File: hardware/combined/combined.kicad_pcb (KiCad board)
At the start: 2 copper layers, 62 x 208.5 mm, 149 parts, among them J1 USB-C 5V in, J2 Mini-DIN-8 to printer, J4 Mini-DIN-8 LocalTalk, SW1 TSB001A3518A, SW2 B3U-1000P, SW3 TS-1002-BR15026, U1 ESP32-S3-WROOM-1-N8R2, U2 SP3490EN-L, U3 SP3232EBEN-L/TR, U4 AP7361C-33E, U5 USBLC6-2SC6, U6 SP3485EN-L, U7 PIC12F1840-I/P, U8 SP3485EN-L, U9 SN74LV1T125DCKR

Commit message: Rev 2026.11: U1 is the ESP32-S3-WROOM-1-N16R8 (W-1091)
Wells picked the N16R8: 16 MB of flash and 8 MB of octal PSRAM against rev
A's 8 MB and 2 MB, so the firmware has room to grow and a job can buffer a
whole photo page. Its PSRAM takes IO35-IO37, which dropping the DIPs freed;
the netlist gate keeps them off every net. It needs its own firmware build
(W-1109) and is rated to 65 C.

r13_sync.py now also copies the Description, Manufacturer and Datasheet
fields, so the board has no field-parity warnings (R9's stale DNP note
went with them).

Refs: W-1091
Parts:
- U1: value ESP32-S3-WROOM-1-N8R2 -> ESP32-S3-WROOM-1-N16R8

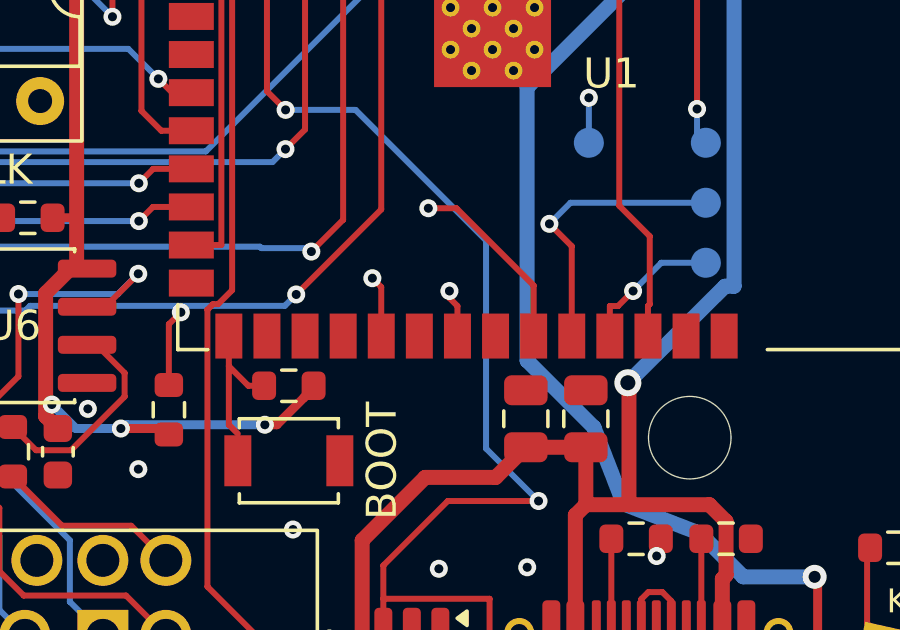
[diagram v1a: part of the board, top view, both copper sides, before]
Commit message: Rev 2026.11: spare pins IO38-IO40 on bare pads; cleanup sees through via stubs (W-1091)
IO38, IO39 and IO40 each run straight down to a via and a bare 1 mm pad on
the back (TP10-TP12, labelled), so a future idea can be tried on a built
board with a few wires. On the back, the front keeps only a short stub per
pin and its ground pour still reaches C1 and C22. IO41 has no way past
USB D- and IO42 has C1 over it.

r13_clean.py no longer counts a stub lying wholly inside a via as joining
it: rev A's DIP and IO35 runs ended so, and the pair held each other up,
leaving dead stubs on IO38, IO40 and IO42. r13_reroute.py's explicit IO35
drops go with it. All other copper is unchanged.

Refs: W-1091
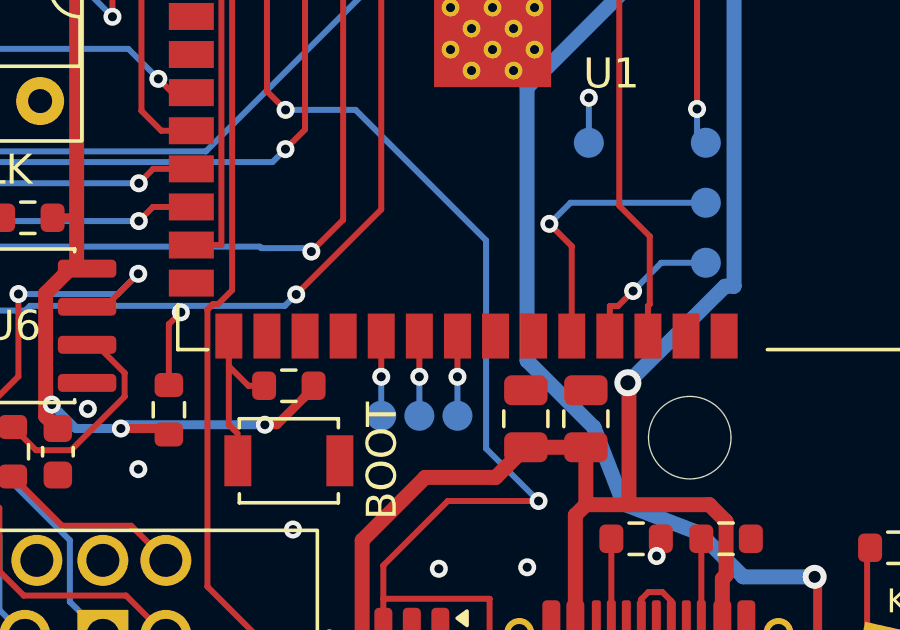
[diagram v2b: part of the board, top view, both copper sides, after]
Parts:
- added TP10: SPARE_IO38, SparePad_D1.0mm, B.Cu at (143.1, 151.2)
- added TP11: SPARE_IO39, SparePad_D1.0mm, B.Cu at (144.3, 151.2)
- added TP12: SPARE_IO40, SparePad_D1.0mm, B.Cu at (145.6, 151.2)
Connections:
- U1 pad 31: unconnected-(U1-IO38-Pad31) -> /SPARE_IO38
- U1 pad 32: unconnected-(U1-IO39-Pad32) -> /SPARE_IO39
- U1 pad 33: unconnected-(U1-IO40-Pad33) -> /SPARE_IO40
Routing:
- net unconnected-(U1-IO42-Pad35): track 6.44 -> 0.00 mm, vias 1 -> 0
- net /SPARE_IO40: track 0.00 -> 2.66 mm, vias 0 -> 1
- net /SPARE_IO39: track 0.00 -> 2.66 mm, vias 0 -> 1
- net /SPARE_IO38: track 0.00 -> 2.66 mm, vias 0 -> 1
- net unconnected-(U1-IO38-Pad31): track 2.25 -> 0.00 mm, vias 1 -> 0
- net unconnected-(U1-IO40-Pad33): track 1.79 -> 0.00 mm, vias 1 -> 0

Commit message: Rev 2026.11: U2 is the THVD1451 (W-1091)
TI's THVD1451DR replaces the SP3490 on the printer port: the same SOIC-8
pinout (checked against TI's SLLSEY3E), +-30 kV HBM on the bus pins
against +-2 kV, and a receiver that works with +-15 V on its inputs, so
an RS-232 printer's line is in range without a divider. R29/R30 stay at
15 k as series protection; a -15 V line lands near -12.5 V. Its
fail-safe threshold reads an idle or unplugged line as mark. Board copper
is unchanged.

Refs: W-1091
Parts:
- U2: value SP3490EN-L -> THVD1451DR

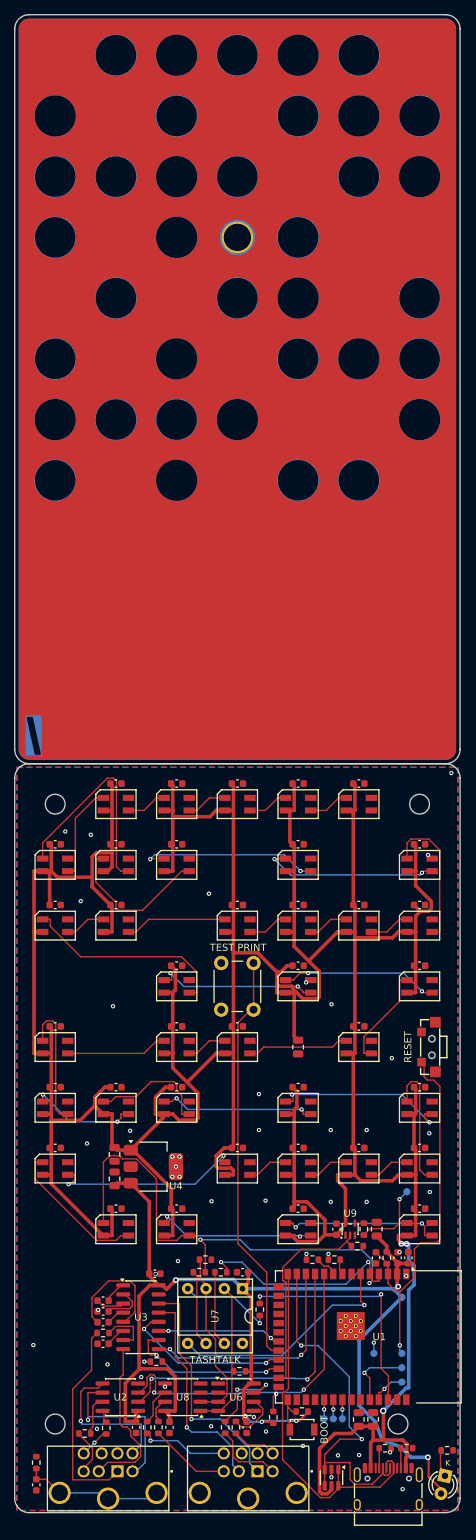
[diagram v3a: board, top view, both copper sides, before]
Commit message: Panel: Frame 16 art, rev 2026.11 (W-1091)
Wells's Frame 16 export, with only its dot area left out: the dots are the
committed ones, pixel for pixel. The rest is Frame 16's: "rev 2026.11", the
text block a few pixels left and up, the port labels on one baseline, and a
power slash of about 1.0 x 5.75 mm (was 0.8 x 5.2), centred 0.3 mm further up.
D3 stays where it is: it can't go west of J1's courtyard, and its 3 mm face
still covers the slash's width. The lattice's D3 tube is re-cut round the new
window (131 tests pass); the combined panel and fab package are rebuilt.

Refs: W-1091
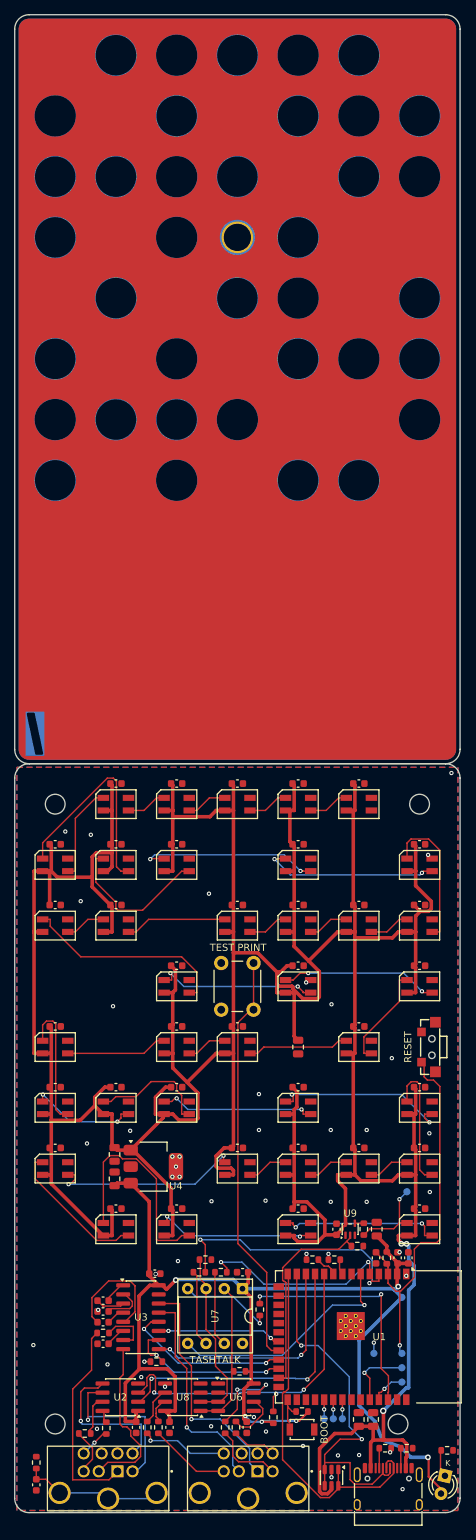
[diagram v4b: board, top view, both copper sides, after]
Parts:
- moved MT2 86.3 mm to (105.6, -38.6)
- moved MT3 86.3 mm to (156.4, 47.7)
- moved MT1 50.7 mm to (156.4, -38.6)
- moved MT4 47.7 mm to (108.6, 47.7)
- renumbered MT2 to MT1, MT4 to MT2, MT1 to MT3, MT3 to MT4

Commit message: Board: WW mark and OSHW logo on the top silk (W-1091)
Where the DIP switch was, at the west edge, where the Lite's clear lid
shows them: the Macintosh Mini board's WW chevrons, 7 mm wide, above
KiCad's 7.5 x 8 mm OSHW logo (a board-only footprint). Copper unchanged;
r13_check.py now checks both are there.

Refs: W-1091
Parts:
- added LOGO1: OSHW-Logo_7.5x8mm_SilkScreen, Symbol:OSHW-Logo_7.5x8mm_SilkScreen, F.Cu at (105.3, 145.4)
